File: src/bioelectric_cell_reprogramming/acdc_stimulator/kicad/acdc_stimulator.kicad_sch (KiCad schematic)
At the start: 55 parts, among them IC1 AD9833BRM-REEL7, IC3 AD5122BCPZ10-RL7, J2 Conn_01x02_Socket, J4 Screw_Terminal_01x02, J5 Conn_ARM_SWD_TagConnect_TC203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, J6 USB_C_Receptacle_USB2.0_14P, Q10 BSZ096N10LS5ATMA1, SW3 SW_Push, SW4 SW_SPDT, U3 AMS1117-3.3, U6 STM32G473RCTx, U7 USBLC6-2SC6, Y2 16Mhz

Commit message: ci: added DC/DC converters to drop 60V to all required power supplies
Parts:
- removed J2: Conn_01x02_Socket, symbol Connector:Conn_01x02_Socket
- added C2: 100nF, Capacitor_SMD:C_0201_0603Metric, symbol Device:C
- added J1: S4B-PH-SM4-TB, male_socket_S4B-PH-SM4-TB.pretty:CONN4_S4B-PH-SM4-TB_JST, symbol 2024-08-13_06-27-45:S4B-PH-SM4-TB
- added J10: Screw_Terminal_01x02, symbol Connector:Screw_Terminal_01x02
- added J3, J9: IPL1-102-01-L-S-K, 1x02_socket_IPL1-102-01-L-S-K.pretty:CONN_IPL1-102-01-L-S-K_SAI, symbol 2024-08-13_01-47-46:IPL1-102-01-L-S-K
- added Q11: NDT3055L, Package_TO_SOT_SMD:SOT-223-3_TabPin2, symbol Transistor_FET:NDT3055L
- added R27, R28: 10k, symbol Device:R
- added R3: 10K, Resistor_SMD:R_0201_0603Metric, symbol Device:R
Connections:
- net +3.3V: now also C2.1, J1.3, R27.2, R28.1, R3.2
- net +60V: now also J10.1 (Pin_1)
- net GND: now also C2.2, J1.2, J10.2 (Pin_2), J3.1, Q11.3 (S)
- net INCUBATOR_PELT_OUT: now reaches U6.10 (PC2)
- net H_BRIDGE_IN1: now reaches U6.11 (PC3)
- net H_BRIDGE_IN2: now reaches U6.22 (PC4)
- net SOLEN_OUT: now reaches U6.23 (PC5)
- net SOLEN_OUT: now also Q11.1 (G)
- net I2C_SCL: now reaches U6.51 (PA15)
- net I2C_SCL: now also J1.1, R27.1
- net I2C_SDA: now reaches U6.60 (PB7)
- net I2C_SDA: now also J1.4, R28.2
- net THERM_FB: now reaches U6.8 (PC0)
- net THERM_FB: now also J3.2, R3.1
- net H_BRIDGE_FAULT: now reaches U6.9 (PC1)
- net SCLK renamed SPI_CLK
- net SDI renamed SPI_DI
- net SDO renamed SPI_DO
- new net +12V: J9.2
- new net CO2 Solenoid: J9.1, Q11.2 (D)
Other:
- added sheet 60_to_12V_converter (60_to_12V_converter.kicad_sch)
- added sheet 60_to_3V3_converter (60_to_3V3_converter.kicad_sch)
- added sheet 60_to_5V_converter (60_to_5V_converter.kicad_sch)
- added sheet pelt_cooler (pelt_cooler.kicad_sch)
- moved on the sheet: C1, C43, C52, C53, C54, C55, C56, J4, L3, L4, Q10, R1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

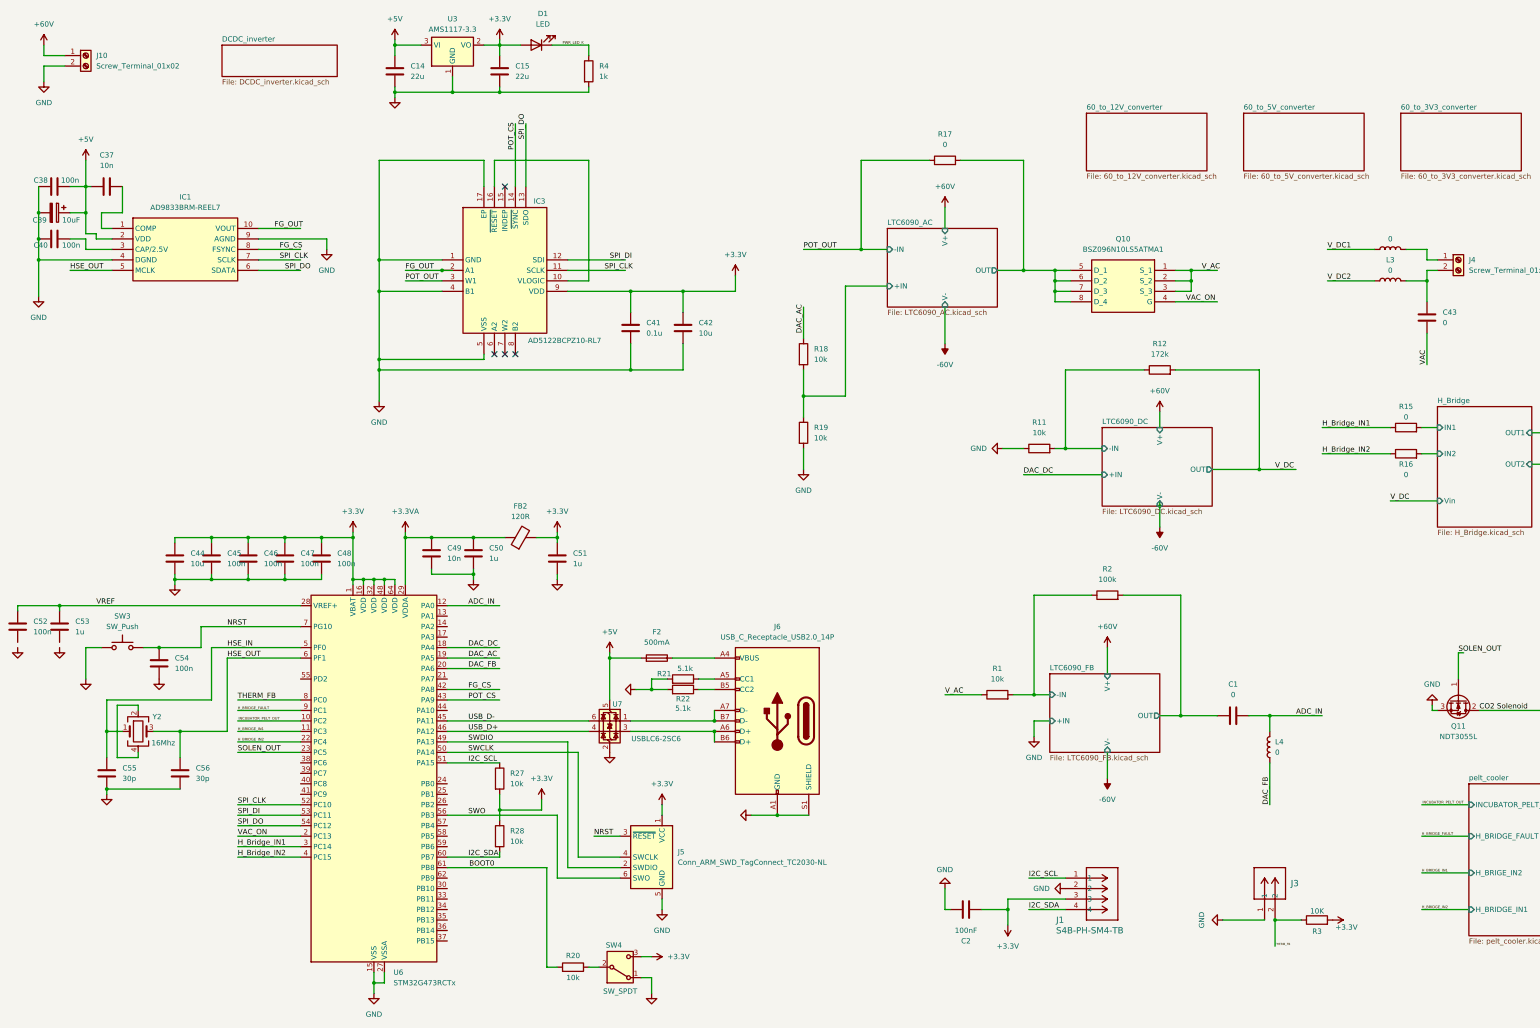
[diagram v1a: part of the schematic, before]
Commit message: CI: footprint assignment done
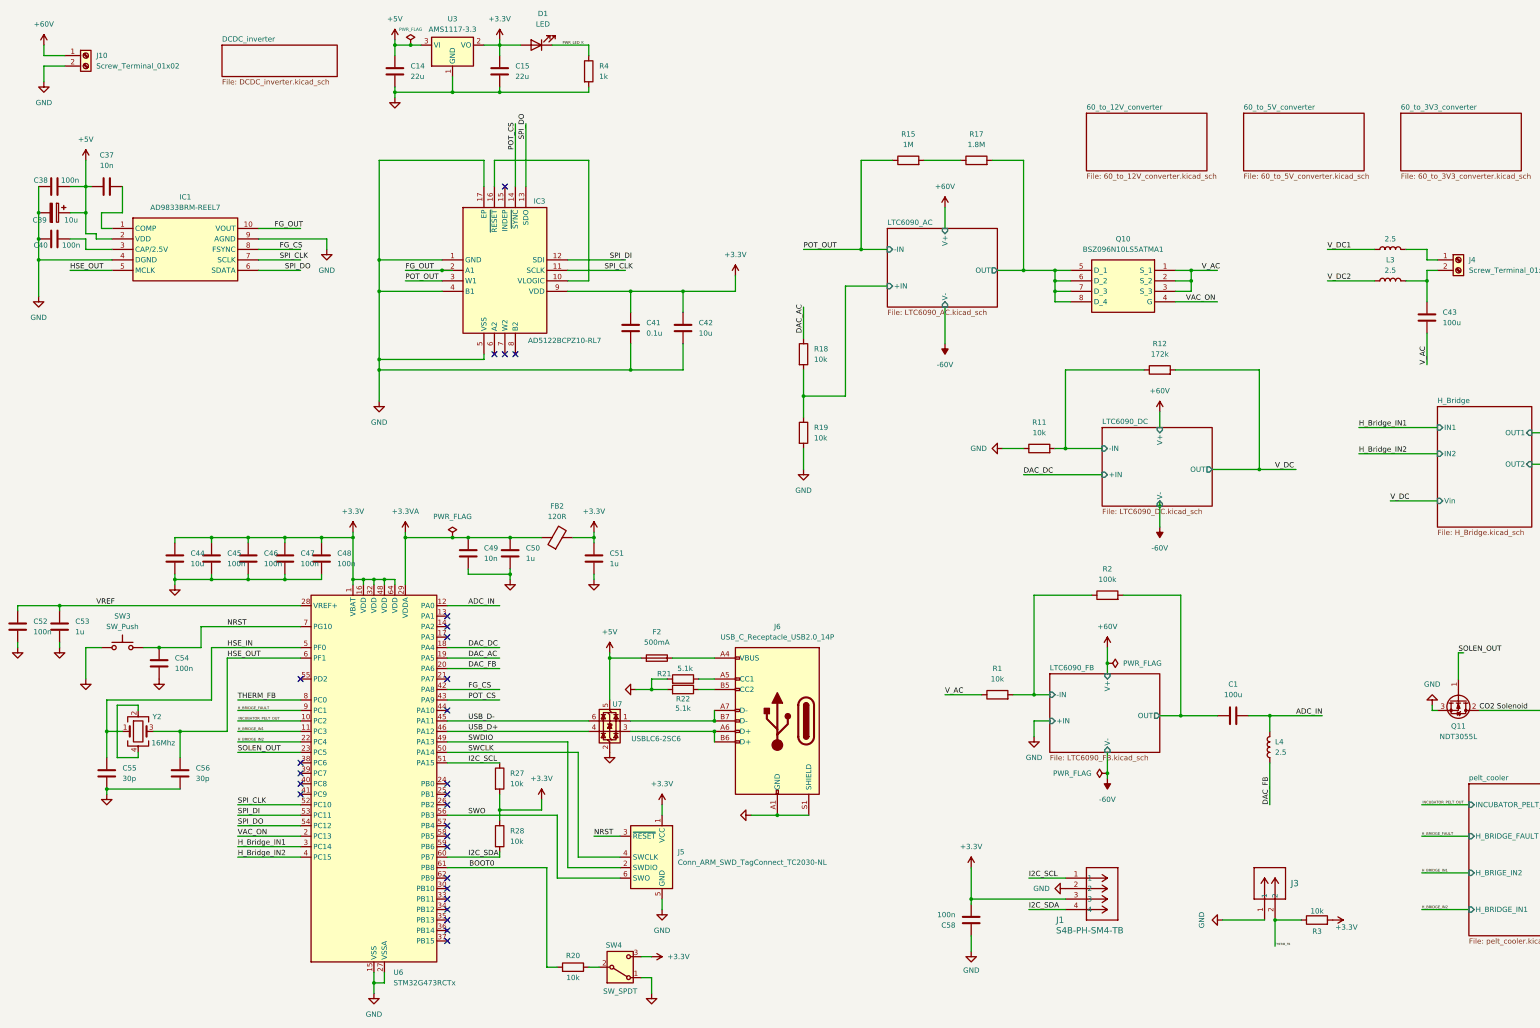
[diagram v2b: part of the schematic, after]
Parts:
- removed C2: 100nF, Capacitor_SMD:C_0201_0603Metric, symbol Device:C
- removed R16: 0, symbol Device:R
- added C58: 100n, Capacitor_SMD:C_0402_1005Metric, symbol Device:C
- C1, C43: value 0 -> 100u; footprint (none) -> Capacitor_THT:C_Disc_D7.5mm_W2.5mm_P5.00mm
- C14, C15: footprint (none) -> Capacitor_SMD:C_0805_2012Metric
- C37, C38, C40, C41, C45, C46, C47, C48, C49, C50, C51, C55, C56: footprint (none) -> Capacitor_SMD:C_0402_1005Metric
- C39: value 10uF -> 10u; footprint (none) -> Capacitor_SMD:CP_Elec_5x5.4
- C42, C44: footprint (none) -> Capacitor_SMD:C_0603_1608Metric
- D1: footprint (none) -> LED_SMD:LED_0402_1005Metric
- FB2: footprint (none) -> Inductor_SMD:L_0603_1608Metric
- IC1: footprint SOP50P490X110-10N -> AD9833BRM-REEL7:SOP50P490X110-10N
- IC3: footprint QFN50P300X300X80-17N-D -> AD5122BCPZ10-RL7:QFN50P300X300X80-17N-D
- J10, J4: footprint (none) -> TerminalBlock:TerminalBlock_Altech_AK300-2_P5.00mm
- L2, L3, L4: value 0 -> 2.5; footprint (none) -> Inductor_THT:L_Radial_D7.0mm_P3.00mm
- Q10: footprint BSZ060NE2LS -> BSZ096N10LS5ATMA1:BSZ060NE2LS
- R1, R11, R18, R19, R20, R27, R28, R4: footprint (none) -> Resistor_SMD:R_0402_1005Metric
- R12, R2: footprint (none) -> Resistor_SMD:R_0603_1608Metric
- R15: value 0 -> 1M; footprint (none) -> Resistor_SMD:R_0805_2012Metric
- R17: value 0 -> 1.8M; footprint (none) -> Resistor_SMD:R_0805_2012Metric
- R3: value 10K -> 10k; footprint Resistor_SMD:R_0201_0603Metric -> Resistor_SMD:R_0402_1005Metric
- SW4: footprint (none) -> Button_Switch_THT:SW_E-Switch_EG1224_SPDT_Angled
- Y2: footprint (none) -> Crystal:Crystal_SMD_3225-4Pin_3.2x2.5mm
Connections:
- net VAC is gone; now on net V_AC: C43.2
- net +3.3V: now also C58.1
- net GND: now also C52.2, C53.2, C58.2
- net H_Bridge_IN1: no longer R15.1
- net POT_OUT: now also R15.1; no longer R17.1
- net H_Bridge/IN1: no longer names the net of R15.2
- net H_Bridge/IN1: now also R17.1
- no-connect marks 4 -> 27
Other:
- moved on the sheet: C49, C50, C51, FB2, R17

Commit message: ci: STM32 layout done and schematic annotated
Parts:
- added C15: 100n, Capacitor_SMD:C_0402_1005Metric, symbol Device:C
- SW1: renamed from SW3; footprint Button_Switch_THT:SW_PUSH-12mm_Wuerth-430476085716 -> Button_Switch_SMD:SW_Push_1P1T_NO_CK_KMR2
- SW2: renamed from SW4; footprint Button_Switch_THT:SW_E-Switch_EG1224_SPDT_Angled -> Button_Switch_SMD:SW_SPDT_PCM12
- renumbered C52 to C1, C54 to C10, C56 to C11, C46 to C12, C47 to C13, C48 to C14, C14 to C16, C49 to C17, C15 to C18, C50 to C19, C38 to C2, C51 to C20, C41 to C21, C42 to C22, C58 to C23, C1 to C24, C43 to C25, C39 to C3, C40 to C4, C53 to C5, C37 to C6, C55 to C7, C44 to C8, C45 to C9, F2 to F1, FB2 to FB1, IC3 to IC2, J10 to J1, J5 to J2, J6 to J3, J1 to J4, J3 to J5, J4 to J6, J9 to J7, L4 to L1, Q10 to Q1, Q11 to Q2, R27 to R1, R17 to R10, R1 to R11, R11 to R12, R2 to R13, R12 to R14, R3 to R15, R28 to R2, R20 to R3, R21 to R5, R22 to R6, R18 to R7, R19 to R8, R15 to R9, U6 to U1, U3 to U2, U7 to U3, Y2 to Y1
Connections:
- net +3.3V: now also C15.1
- net GND: now also C15.2
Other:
- note added: "AC Generation"
- note added: "DC Offset Generation and Signal Output"
- note added: "Incubator Peripherals"
- note added: "Power Supplies"
- note added: "STM32, USB/SWD Bus"
- moved on the sheet: C1, C10, C11, C12, C13, C14, C16, C17, C18, C19, C2, C20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

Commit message: GND vias added
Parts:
- added H1, H2, H3, H4: MountingHole, MountingHole:MountingHole_2.7mm_M2.5, symbol Mechanical:MountingHole
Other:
- note added: "Mounting Holes(M2)"

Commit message: ci: adding LTspice files
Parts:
- R11: value 10k -> 1k
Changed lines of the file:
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@@
 			)
 		)
-		(property "Value" "10k"
+		(property "Value" "1k"
 			(at 116.84 111.76 90)
 			(effects

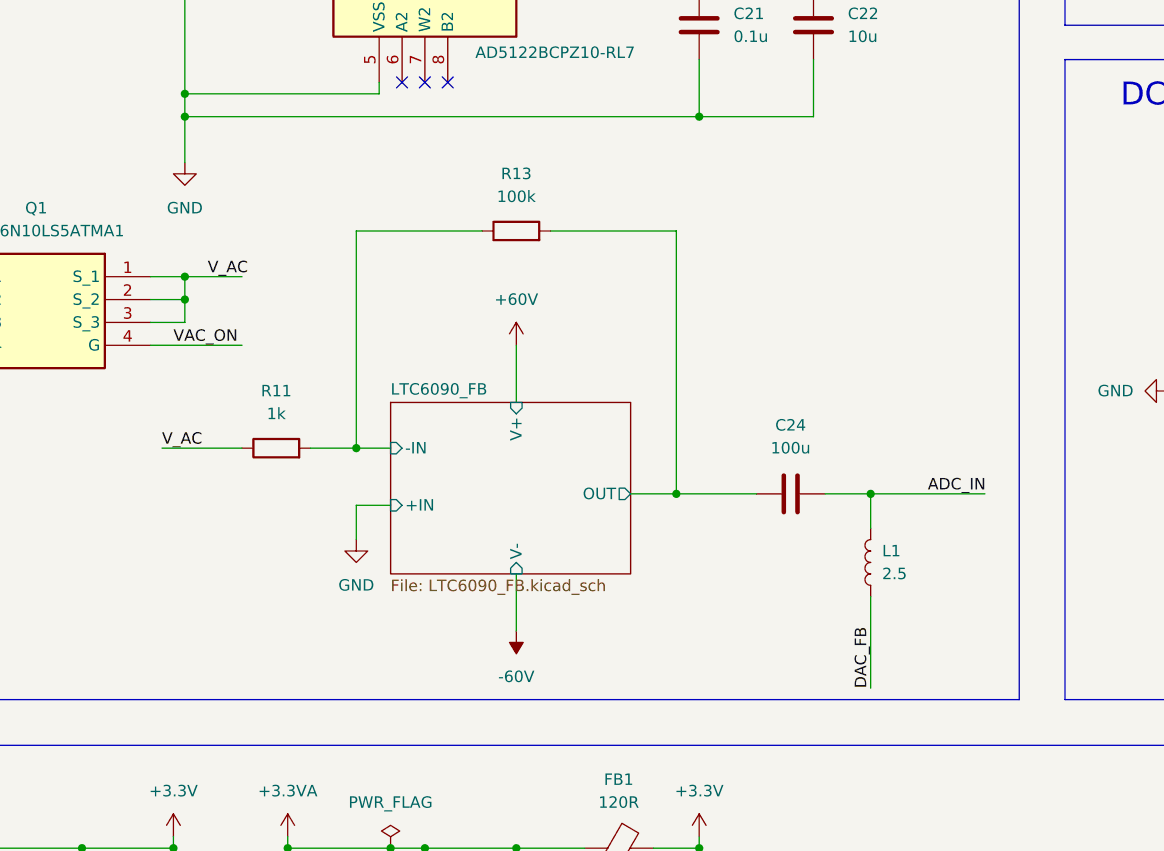
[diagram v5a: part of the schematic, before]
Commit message: fix: replaced op amp with voltage divider for ADC
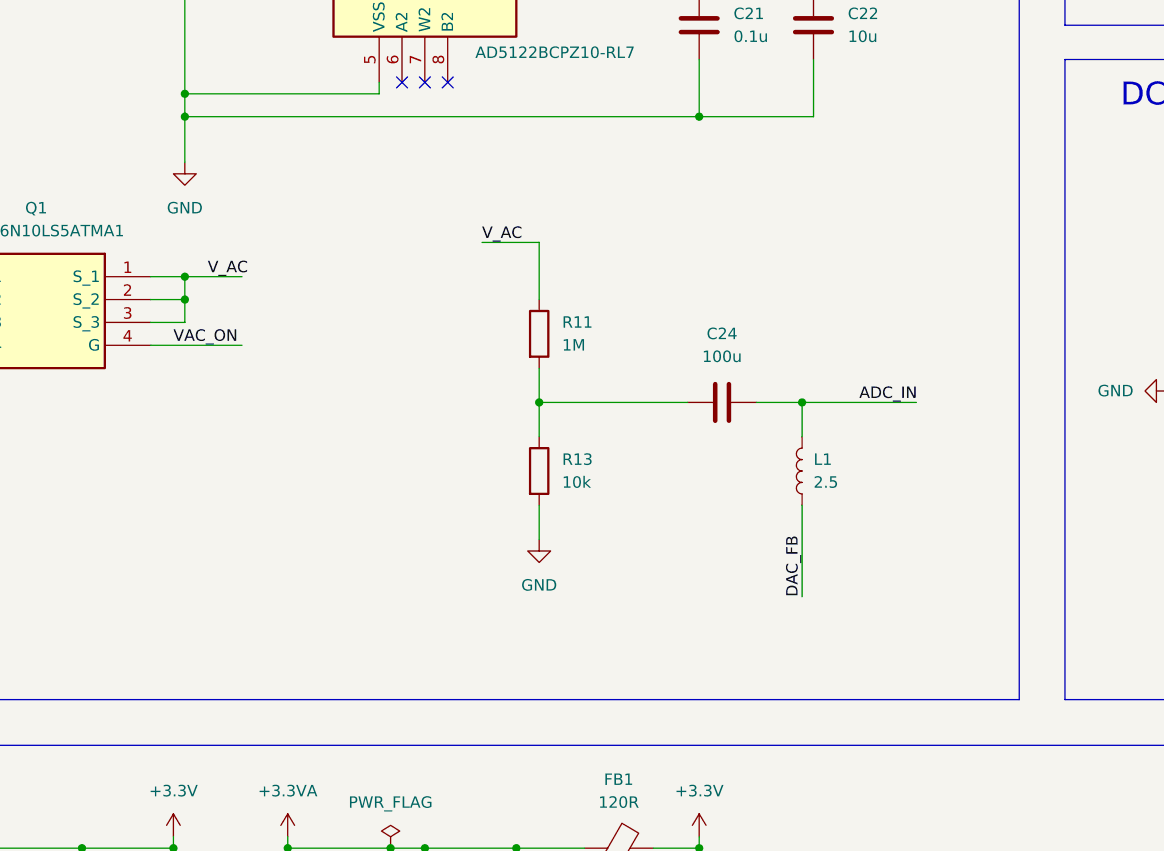
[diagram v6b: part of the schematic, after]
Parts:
- R11: value 1k -> 1M; footprint Resistor_SMD:R_0402_1005Metric -> Resistor_SMD:R_0603_1608Metric
- R13: value 100k -> 10k; footprint Resistor_SMD:R_0603_1608Metric -> Resistor_SMD:R_0402_1005Metric
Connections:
- net GND: now also R13.2
- net LTC6090_FB/-IN: no longer names the net of R11.2, R13.1
- net LTC6090_FB/-IN: now also C24.1
- removed net LTC6090_FB/OUT: C24.1, R13.2
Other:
- removed sheet LTC6090_FB
- moved on the sheet: C24, L1

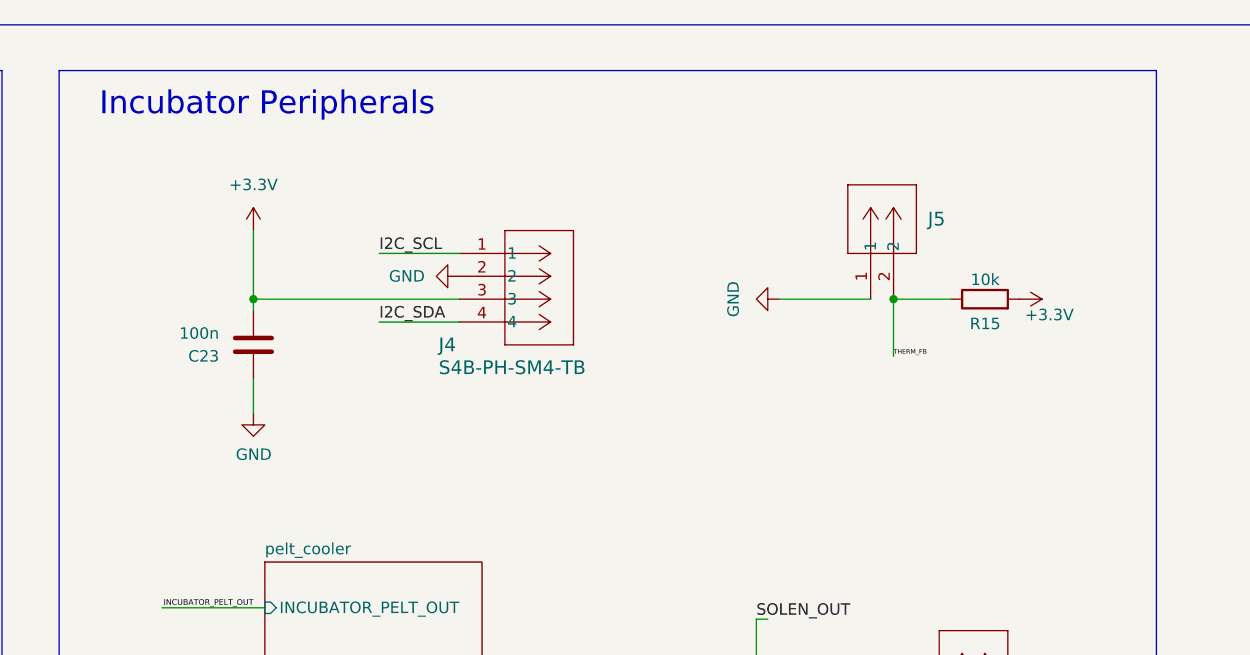
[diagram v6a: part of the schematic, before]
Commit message: finished routing power supplies
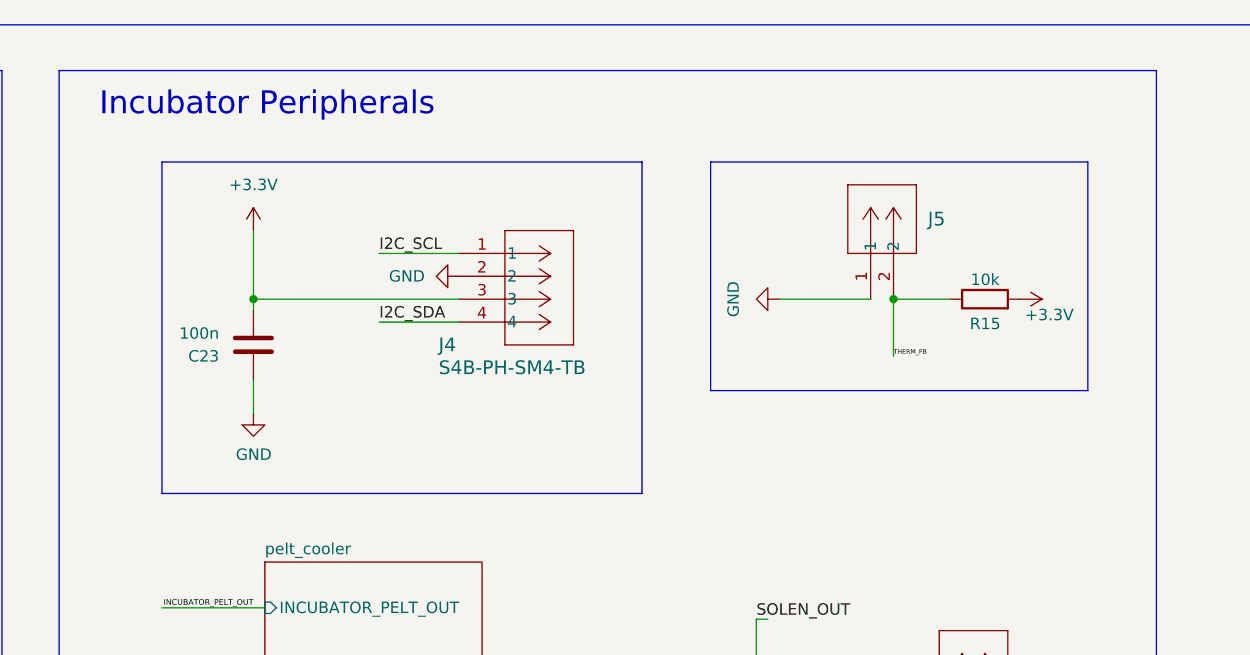
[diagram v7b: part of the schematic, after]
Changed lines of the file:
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@@
+		)
+	)
+	(polyline
+		(pts
+			(xy 242.57 195.58) (xy 295.91 195.58)
+		)
+		(stroke
+			(width 0)
+			(type default)
 		)
 	)
@@
 		)
 	)
+	(polyline
+		(pts
+			(xy 303.53 158.75) (xy 303.53 184.15)
+		)
+		(stroke
+			(width 0)
+			(type default)
+		)
+	)
 	(wire
 		(pts
@@
 		)
 	)
+	(polyline
+		(pts
+			(xy 295.91 195.58) (xy 295.91 158.75)
+		)
+		(stroke
+			(width 0)
+			(type default)
+		)
+	)
 	(wire
 		(pts
@@
 		)
 	)
+	(polyline
+		(pts
+			(xy 303.53 184.15) (xy 345.44 184.15)
+		)
+		(stroke
+			(width 0)
+			(type default)
+		)
+	)
 	(wire
 		(pts
@@
 	(polyline
 		(pts
+			(xy 345.44 184.15) (xy 345.44 158.75)
+		)
+		(stroke
+			(width 0)
+			(type default)
+		)
+	)
+	(polyline
+		(pts
 			(xy 378.46 15.24) (xy 378.46 68.58)
 		)
@@
 		)
 	)
+	(polyline
+		(pts
+			(xy 242.57 158.75) (xy 242.57 195.58)
+		)
+		(stroke
+			(width 0)
+			(type default)
+		)
+	)
 	(wire
 		(pts
@@
 		)
 	)
+	(polyline
+		(pts
+			(xy 242.57 158.75) (xy 295.91 158.75)
+		)
+		(stroke
+			(width 0)
+			(type default)
+		)
+	)
 	(wire
 		(pts
@@
 		)
 		(stroke
+			(width 0)
+			(type default)
+		)
+	)
+	(polyline
+		(pts
+			(xy 303.53 158.75) (xy 345.44 158.75)
+		)
+		(stroke

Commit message: fixed some more clearance errors
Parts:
- C1, C10, C12, C13, C14, C15, C2, C23, C4, C9: Distributor Link (none) -> https://jlcpcb.com/partdetail/173559-GRM155R62A104KE14D/C16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; Manufacturer (none) -> Murata Electronics; Manufacturer Part Number (none) -> GRM155R62A104KE14D
- R1, R12, R13, R15, R2, R3, R7, R8: Distributor Link (none) -> https://jlcpcb.com/partdetail/259901-NQ02WGJ0103TCE/C270371; Manufacturer (none) -> UNI-ROYAL(Uniroyal Elec); Manufacturer Part Number (none) -> NQ02WGJ0103TCE
